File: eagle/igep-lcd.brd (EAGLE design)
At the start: 108.9 x 83.8 mm, 68 parts, among them IC1 LM1117IMPX-3.3, U1 SN74LVC8T245PW, U2 SN74LVC8T245PW, U3 SN74LVC8T245PW, U4 SN74LVC8T245PW

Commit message: Developing PCB design...
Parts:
- moved C37 80.1 mm to (96.5, 31.8), flipped to the bottom, turned to 270 degrees
- moved C21 78.0 mm to (94.0, 17.8), flipped to the bottom, turned to 270 degrees
- moved C29 76.8 mm to (92.7, 24.1), turned to 270 degrees
- moved C36 70.7 mm to (94.0, 30.5), flipped to the bottom, turned to 270 degrees
- moved C20 68.7 mm to (91.4, 16.5), flipped to the bottom, turned to 270 degrees
- moved C28 67.5 mm to (90.2, 22.9), turned to 270 degrees
- moved C19 63.1 mm to (90.2, 10.2), flipped to the bottom, turned to 180 degrees
- moved C35 61.6 mm to (91.4, 29.2), flipped to the bottom, turned to 270 degrees
- moved U3 61.4 mm to (78.7, 34.3)
- moved C18 58.8 mm to (91.4, 7.62), flipped to the bottom, turned to 180 degrees
- moved C27 58.5 mm to (87.6, 21.6), turned to 270 degrees
- moved C17 55.1 mm to (92.7, 5.08), flipped to the bottom, turned to 180 degrees
- moved C40 53.6 mm to (88.9, 15.2), flipped to the bottom, turned to 270 degrees
- moved C34 52.8 mm to (88.9, 27.9), flipped to the bottom, turned to 270 degrees
- moved C16 52.1 mm to (94.0, 2.54), flipped to the bottom, turned to 180 degrees
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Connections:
- new net N$12: R5.1, U$7.TS2
- new net N$18: R3.1, U$7.TS1
- new net N$19: R10.1, U$4.EN
- new net N$24: R9.1, U$3.EN
- new net N$28: R8.1, U$2.EN
- new net N$3: R7.1, U$7.TS4
- new net N$30: C38.1, U3.21
- new net N$32: C37.1, U3.20
- new net N$37: C36.1, U3.19
- new net N$38: C35.1, U3.18
- new net N$39: C34.1, U3.17
- new net N$40: C33.1, U3.16
- new net N$41: C32.1, U3.15
- new net N$42: C31.1, U3.14
- new net N$43: C30.1, U2.21
- new net N$44: C29.1, U2.20
- new net N$45: C28.1, U2.19
- new net N$46: C27.1, U2.18
- new net N$47: C26.1, U2.17
- new net N$48: C25.1, U2.16
- new net N$49: C23.1, U2.15
- new net N$50: C24.1, U2.14
- new net N$51: C22.1, U1.21
- new net N$52: C21.1, U1.20
- new net N$53: C20.1, U1.19
- new net N$54: C19.1, U1.18
- new net N$55: C18.1, U1.17
- new net N$56: C17.1, U1.16
- new net N$57: C16.1, U1.15
- new net N$58: C40.1, U1.14
- new net N$6: R6.1, U$7.TS3
- net LCD_DATA0: no longer C22.1, U1.21
- net LCD_DATA1: no longer C21.1, U1.20
- net LCD_DATA10: no longer C28.1, U2.19
- net LCD_DATA11: no longer C27.1, U2.18
- net LCD_DATA12: no longer C26.1, U2.17
- net LCD_DATA13: no longer C25.1, U2.16
- net LCD_DATA14: no longer C23.1, U2.15
- net LCD_DATA15: no longer C24.1, U2.14
- net LCD_DATA16: no longer C38.1, U3.21
- net LCD_DATA17: no longer C37.1, U3.20
- net LCD_DATA18: no longer C36.1, U3.19
- net LCD_DATA19: no longer C35.1, U3.18
- net LCD_DATA2: no longer C20.1, U1.19
- net LCD_DATA20: no longer C34.1, U3.17
- net LCD_DATA21: no longer C33.1, U3.16
- net LCD_DATA22: no longer C32.1, U3.15
- net LCD_DATA23: no longer C31.1, U3.14
- net LCD_DATA3: no longer C19.1, U1.18
- net LCD_DATA4: no longer C18.1, U1.17
- net LCD_DATA5: no longer C17.1, U1.16
- net LCD_DATA6: no longer C16.1, U1.15
- net LCD_DATA7: no longer C40.1, U1.14
- net LCD_DATA8: no longer C30.1, U2.21
- net LCD_DATA9: no longer C29.1, U2.20
- net N$29: no longer R3.1, U$7.TS1
- net N$31: no longer R5.1, U$7.TS2
- net N$33: no longer R6.1, U$7.TS3
- net N$34: no longer R7.1, U$7.TS4
- net N$35: no longer R10.1, R8.1, R9.1, U$2.EN, U$3.EN, U$4.EN

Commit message: First phase of PCD design
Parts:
- moved C7 87.5 mm to (20.3, 22.9), flipped to the top, turned to 0 degrees
- moved U$6 69.9 mm to (22.9, 14.0)
- moved C9 56.8 mm to (25.4, 7.62), turned to 180 degrees
- moved C10 45.8 mm to (20.3, 25.4)
- moved C14 33.0 mm to (54.6, 5.08)
- moved C11 32.2 mm to (5.08, 44.5)
- moved IC1 32.2 mm to (5.08, 44.5)
- moved C1 32.0 mm to (3.81, 35.6)
- moved C2 32.0 mm to (3.81, 38.1)
- moved C3 30.5 mm to (76.2, 49.5), flipped to the top, turned to 90 degrees
- moved C15 29.3 mm to (81.3, 49.5), turned to 270 degrees
- moved R10 27.4 mm to (86.4, 52.1), turned to 90 degrees
- moved U1 23.0 mm to (47.0, 7.62)
- moved U$5 22.9 mm to (101.6, 55.9)
- moved D1 21.9 mm to (99.1, 59.7), turned to 90 degrees
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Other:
- board size 108.9 x 83.8 mm -> 108.9 x 68.6 mm

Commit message: First routed version of the PCB
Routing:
- net N$2: track 0.00 -> 387.7 mm, vias 0 -> 4
- net N$36: track 0.00 -> 258.2 mm, vias 0 -> 1
- net N$35: track 0.00 -> 214.4 mm, vias 0 -> 5
- net N$4: track 0.00 -> 145.2 mm, vias 0 -> 2
- net VSYNC: track 0.00 -> 93.6 mm, vias 0 -> 1
- net DEN: track 0.00 -> 90.8 mm, vias 0 -> 3
- net IGEP_LCD_DATA16: track 0.00 -> 90.5 mm, vias 0 -> 1
- net PCLK: track 0.00 -> 88.4 mm, vias 0 -> 3
- net HSYNC\: track 0.00 -> 88.3 mm, vias 0 -> 1
- net IGEP_LCD_DATA18: track 0.00 -> 87.6 mm, vias 0 -> 1
- net IGEP_LCD_DATA20: track 0.00 -> 84.5 mm, vias 0 -> 1
- net IGEP_LCD_DATA22: track 0.00 -> 82.2 mm, vias 0 -> 1
- net N$33: track 0.00 -> 80.9 mm
- net N$29: track 0.00 -> 80.0 mm
- net N$31: track 0.00 -> 79.5 mm
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
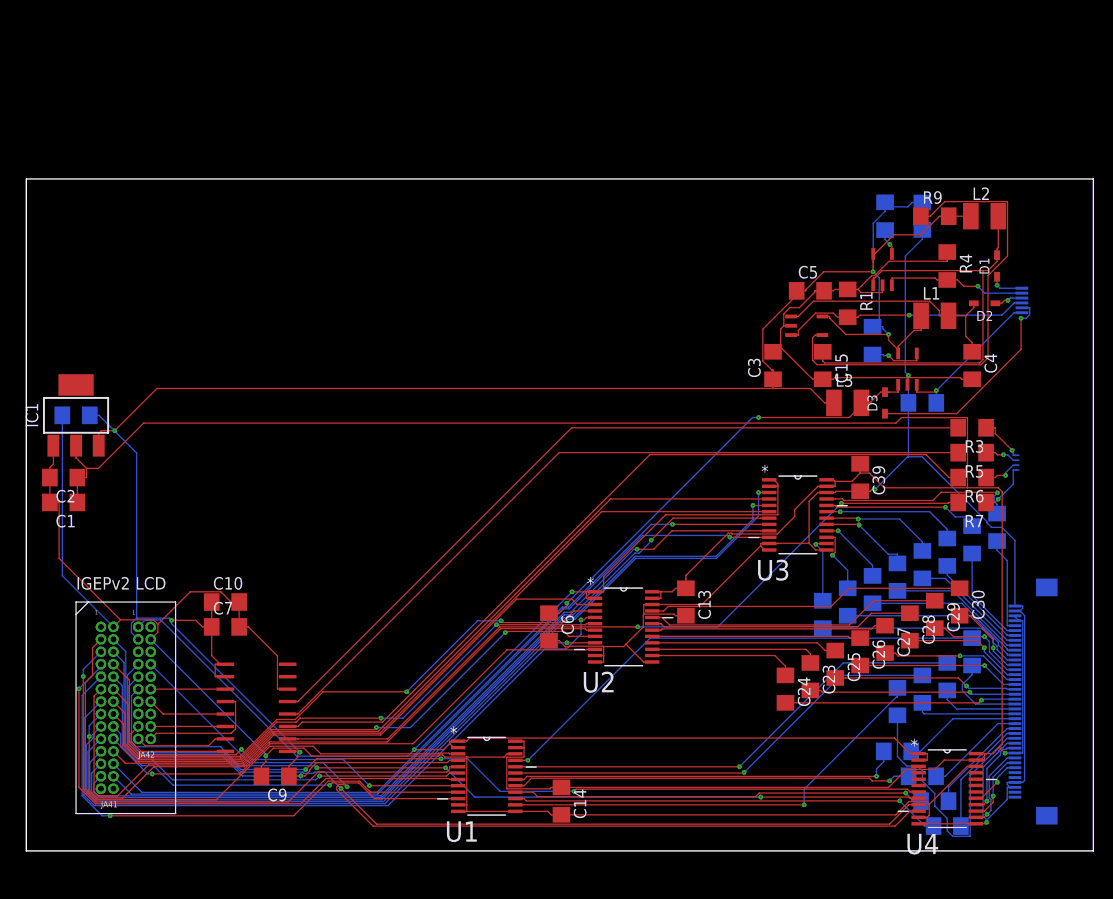
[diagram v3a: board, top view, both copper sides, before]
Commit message: PCB layout phase 2 done
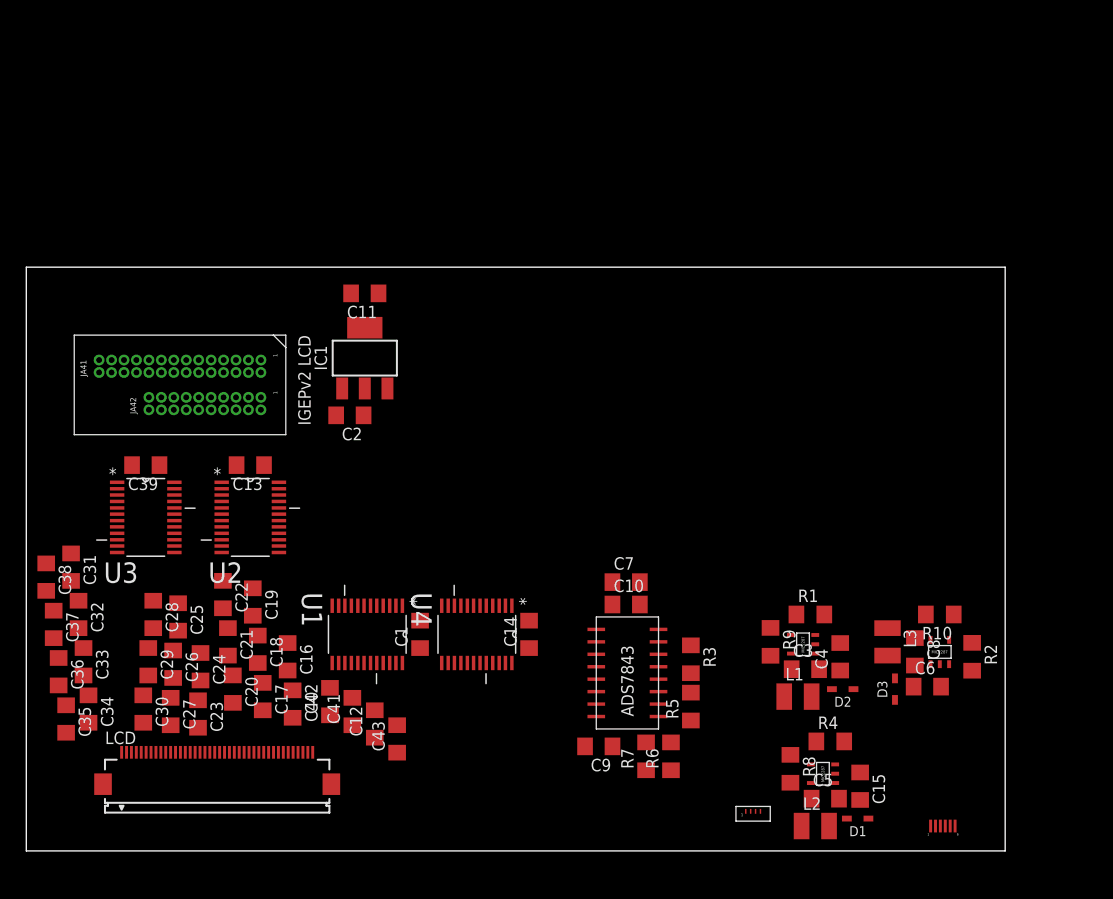
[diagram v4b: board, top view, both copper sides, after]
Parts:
- added C12, C41, C42, C43: 100nF, rcl:C1206
- moved C38 97.2 mm to (2.03, 27.9), flipped to the top
- moved C37 94.1 mm to (2.79, 23.1), flipped to the top
- moved C36 91.5 mm to (3.30, 18.3), flipped to the top
- moved C35 88.8 mm to (4.06, 13.5), flipped to the top
- moved LCD 85.1 mm to (19.5, 6.81), flipped to the top, turned to 0 degrees
- moved C30 84.0 mm to (11.9, 14.5)
- moved C34 83.6 mm to (6.35, 14.5), flipped to the top
- moved C33 80.9 mm to (5.84, 19.3), flipped to the top
- moved C29 80.4 mm to (12.4, 19.3)
- moved C32 78.5 mm to (5.33, 24.1), flipped to the top
- moved C28 77.2 mm to (13.0, 24.1)
- moved C31 76.9 mm to (4.57, 29.0), flipped to the top
- moved C22 76.7 mm to (20.1, 26.2), flipped to the top
- moved C21 73.5 mm to (20.6, 21.3), flipped to the top
- moved C27 73.3 mm to (14.7, 14.2)
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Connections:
- net N$10: now also C42.1, C42.2
- net N$11: now also C43.1, C43.2
- net N$5: now also C41.1, C41.2
- net N$9: now also C12.1, C12.2
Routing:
- net N$2: track 387.7 -> 0.00 mm, vias 4 -> 0
- net N$36: track 258.2 -> 0.00 mm, vias 1 -> 0
- net N$35: track 214.4 -> 0.00 mm, vias 5 -> 0
- net N$4: track 145.2 -> 0.00 mm, vias 2 -> 0
- net VSYNC: track 93.6 -> 0.00 mm, vias 1 -> 0
- net DEN: track 90.8 -> 0.00 mm, vias 3 -> 0
- net IGEP_LCD_DATA16: track 90.5 -> 0.00 mm, vias 1 -> 0
- net PCLK: track 88.4 -> 0.00 mm, vias 3 -> 0
- net HSYNC\: track 88.3 -> 0.00 mm, vias 1 -> 0
- net IGEP_LCD_DATA18: track 87.6 -> 0.00 mm, vias 1 -> 0
- net IGEP_LCD_DATA20: track 84.5 -> 0.00 mm, vias 1 -> 0
- net IGEP_LCD_DATA22: track 82.2 -> 0.00 mm, vias 1 -> 0
- net N$33: track 80.9 -> 0.00 mm
- net N$29: track 80.0 -> 0.00 mm
- net N$31: track 79.5 -> 0.00 mm
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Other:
- board size 108.9 x 68.6 mm -> 99.9 x 59.6 mm

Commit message: Added routing + ground plates + holes
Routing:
- net N$2: track 0.00 -> 324.5 mm
- net N$35: track 0.00 -> 153.9 mm
- net N$36: track 0.00 -> 108.1 mm, vias 0 -> 3
- net N$4: track 0.00 -> 84.6 mm, vias 0 -> 1
- net N$1: track 0.00 -> 63.9 mm, vias 0 -> 1
- net N$7: track 0.00 -> 60.6 mm, vias 0 -> 1
- net N$27: track 0.00 -> 58.8 mm, vias 0 -> 1
- net N$26: track 0.00 -> 57.1 mm, vias 0 -> 1
- net N$25: track 0.00 -> 55.4 mm, vias 0 -> 1
- net N$20: track 0.00 -> 53.7 mm, vias 0 -> 1
- net IGEP_LCD_DATA8: track 0.00 -> 47.6 mm, vias 0 -> 1
- net IGEP_LCD_DATA10: track 0.00 -> 43.8 mm, vias 0 -> 1
- net IGEP_LCD_DATA12: track 0.00 -> 40.9 mm, vias 0 -> 1
- net PCLK: track 0.00 -> 40.3 mm, vias 0 -> 1
- net DEN: track 0.00 -> 39.3 mm, vias 0 -> 1
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- added copper zone on layer 1, net N$59
- added copper zone on layer 16, net N$60

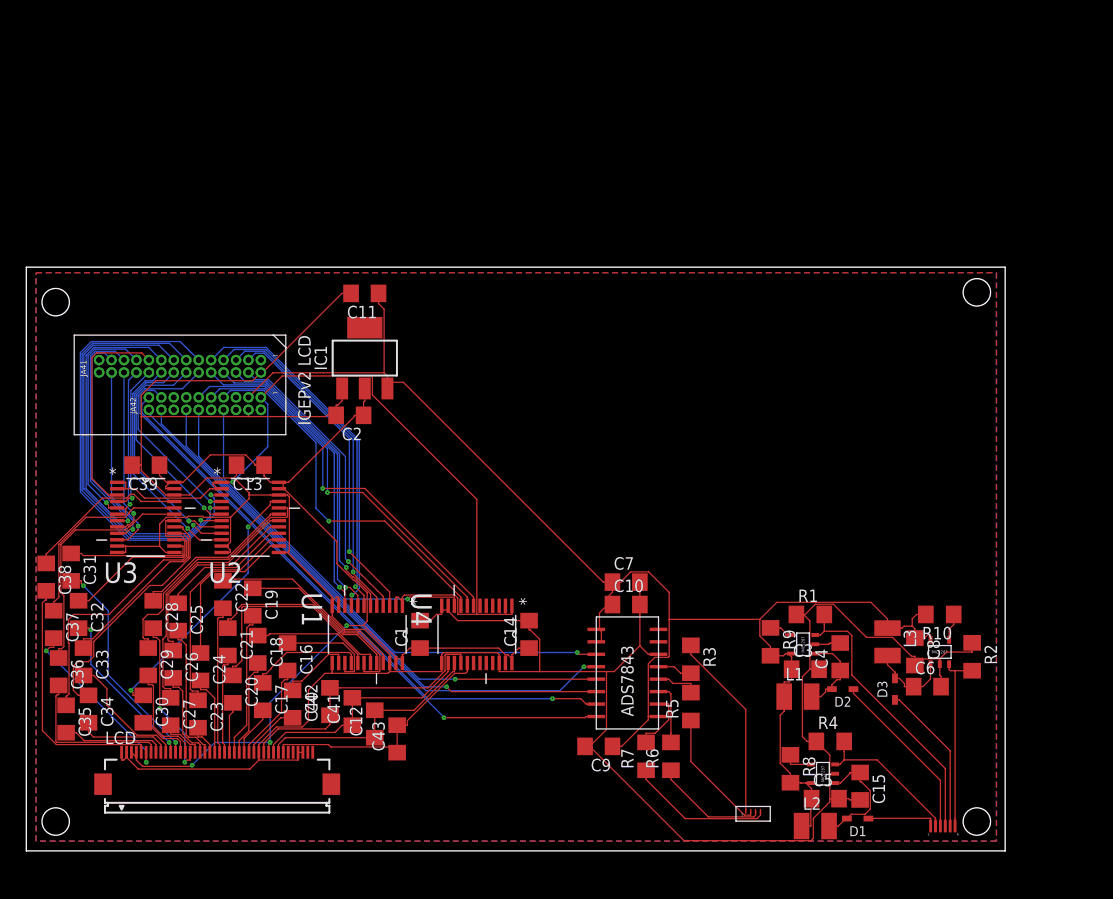
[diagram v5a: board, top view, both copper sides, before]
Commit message: Wider power lines for LCD backlight
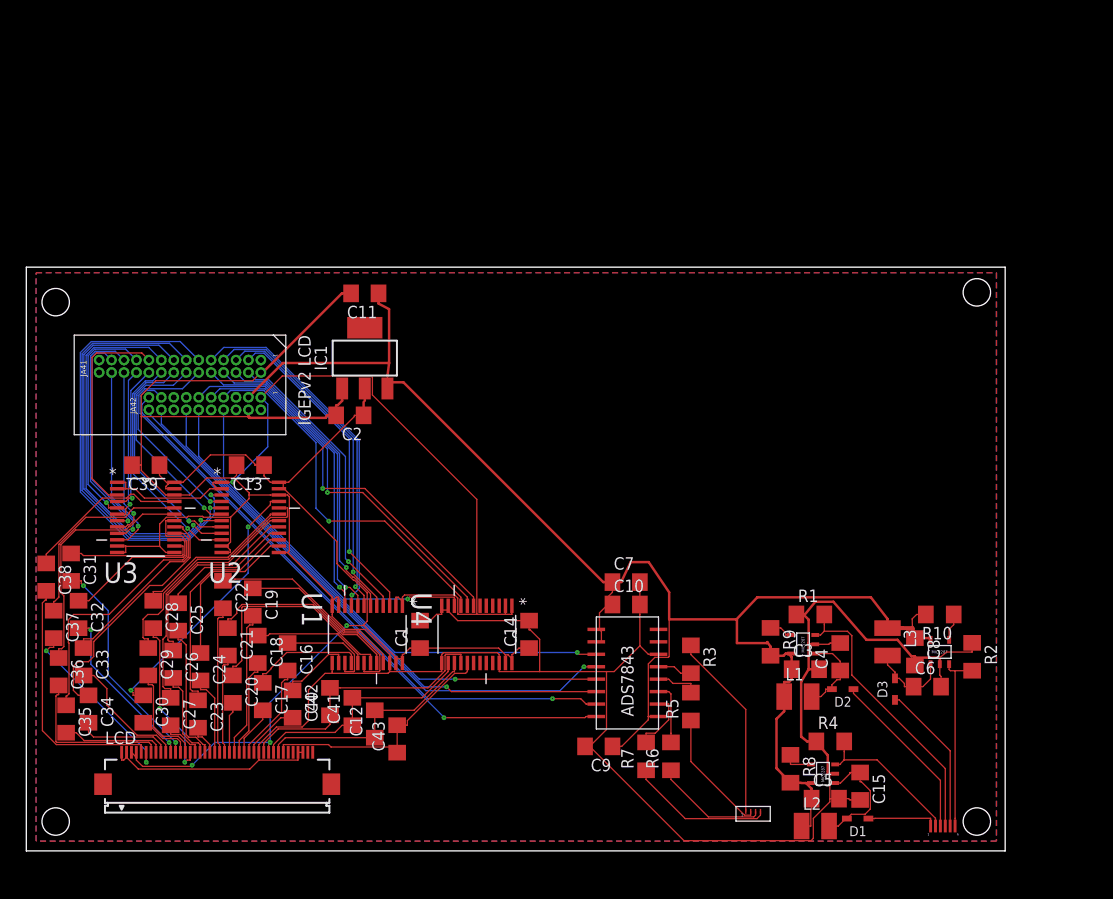
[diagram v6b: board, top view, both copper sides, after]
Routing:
- net N$35: track 153.9 -> 159.9 mm
- net N$2: track 324.5 -> 325.8 mm
